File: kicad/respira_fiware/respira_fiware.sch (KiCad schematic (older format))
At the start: 14 parts, among them J1 AC PWR, J2 ES1-NO2, J3 SI7021, J4 RJ45, J5 SPS30, J6 DC PWR, U1 ESP32-NODEMCU, U2 myrra_48022

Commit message: Updating connectors and main SoC
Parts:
- J1, J6: symbol respira_fiware-rescue:Conn_01x02-gateway-rescue-gateway-rescue -> Connector_Generic:Conn_01x02
- U1: symbol respira_fiware-rescue:ESP32-NODEMCU-panstamp-gateway-rescue -> panstamp:ESP32-NODEMCU
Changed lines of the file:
@@
 $EndDescr
 $Comp
-L respira_fiware-rescue:Conn_01x02-gateway-rescue-gateway-rescue J1
+L Connector_Generic:Conn_01x02 J1
 U 1 1 5B6D72CF
 P 2000 6250
@@
 TXD0
 $Comp
-L respira_fiware-rescue:ESP32-NODEMCU-panstamp-gateway-rescue U1
+L panstamp:ESP32-NODEMCU U1
 U 1 1 5BADDDF2
 P 3200 3350
@@
 ESP32 NODEMCU board
 $Comp
-L respira_fiware-rescue:Conn_01x02-gateway-rescue-gateway-rescue J6
+L Connector_Generic:Conn_01x02 J6
 U 1 1 5D5DC69E
 P 2000 6700

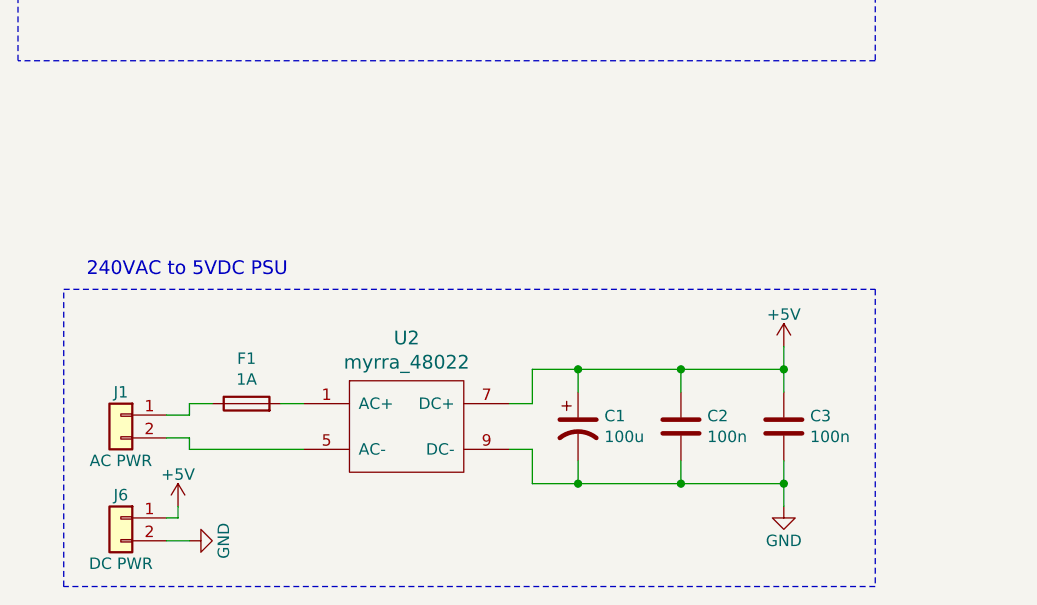
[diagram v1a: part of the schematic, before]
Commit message: Removing AC parts
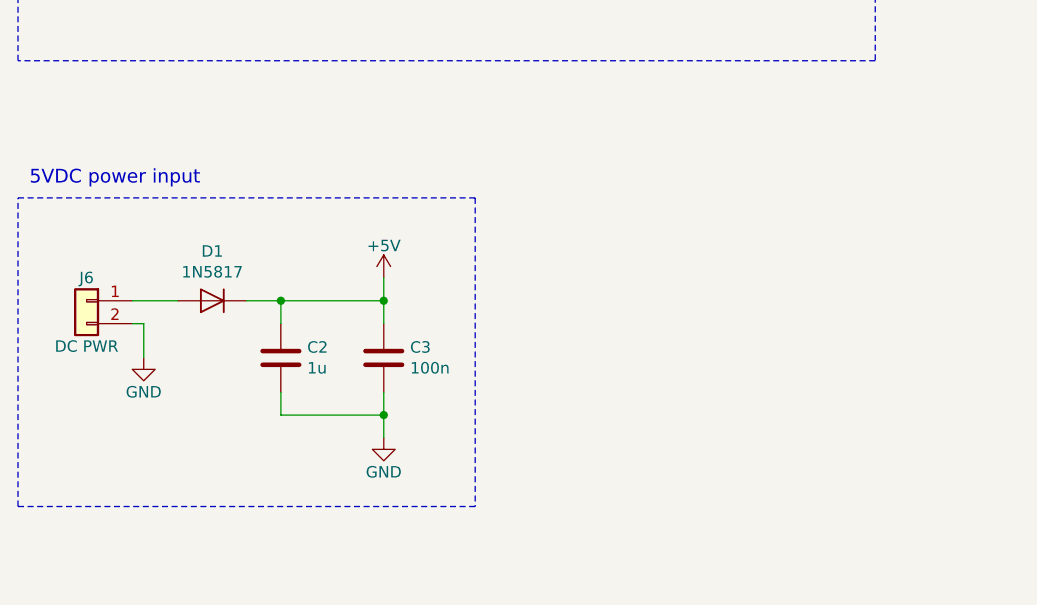
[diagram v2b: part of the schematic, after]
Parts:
- removed C1: 100u, Capacitor_THT:CP_Radial_D6.3mm_P2.50mm, symbol Device:CP1
- removed F1: 1A, mymods:litefuse_646, symbol Device:Fuse
- removed J1: AC PWR, myconnectors:terminal_block_5mm_2P, symbol Connector_Generic:Conn_01x02
- removed U2: myrra_48022, mymods:myrra_48022, symbol panstamp:myrra_48022
- added D1: 1N5817, Diode_THT:D_DO-41_SOD81_P10.16mm_Horizontal, symbol Device:D
- C2: value 100n -> 1u
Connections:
- net +5V: now also D1.1 (K); no longer J6.1 (Pin_1)
- new net: D1.2 (A), J6.1 (Pin_1)
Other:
- note added: "5VDC power input"
- note removed: "240VAC to 5VDC PSU"
- moved on the sheet: C2, C3, J6
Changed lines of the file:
@@
 $EndDescr
-$Comp
-L Connector_Generic:Conn_01x02 J1
-U 1 1 5B6D72CF
-P 2000 6250
-F 0 "J1" H 2000 6350 50  0000 C CNN
-F 1 "AC PWR" H 2000 6050 50  0000 C CNN
-F 2 "myconnectors:terminal_block_5mm_2P" H 2000 6250 50  0001 C CNN
-F 3 "" H 2000 6250 50  0001 C CNN
-	1    2000 6250
-	-1   0    0    -1
-$EndComp
 $Comp
 L power:+5V #PWR02
@@
 I2C_SDA
 $Comp
-L panstamp:myrra_48022 U2
-U 1 1 5D5AAFF8
-P 3250 6300
-F 0 "U2" H 3250 6687 60  0000 C CNN
-F 1 "myrra_48022" H 3250 6581 60  0000 C CNN
-F 2 "mymods:myrra_48022" H 3250 6300 60  0001 C CNN
-F 3 "" H 3250 6300 60  0001 C CNN
-	1    3250 6300
-	1    0    0    -1
-$EndComp
-$Comp
-L Device:Fuse F1
-U 1 1 5D5AE5C1
-P 2550 6200
-F 0 "F1" V 2747 6200 50  0000 C CNN
-F 1 "1A" V 2656 6200 50  0000 C CNN
-F 2 "mymods:litefuse_646" V 2480 6200 50  0001 C CNN
-F 3 "~" H 2550 6200 50  0001 C CNN
-	1    2550 6200
-	0    -1   -1   0
-$EndComp
-Wire Wire Line
-	2700 6200 2800 6200
-Wire Wire Line
-	2400 6200 2300 6200
-Wire Wire Line
-	2300 6200 2300 6250
-Wire Wire Line
-	2300 6250 2200 6250
-Wire Wire Line
-	2200 6350 2300 6350
-Wire Wire Line
-	2300 6350 2300 6400
-Wire Wire Line
-	2300 6400 2800 6400
-$Comp
-L Device:CP1 C1
-U 1 1 5D5AED16
-P 4000 6300
-F 0 "C1" H 4115 6346 50  0000 L CNN
-F 1 "100u" H 4115 6255 50  0000 L CNN
-F 2 "Capacitor_THT:CP_Radial_D6.3mm_P2.50mm" H 4000 6300 50  0001 C CNN
-F 3 "~" H 4000 6300 50  0001 C CNN
-	1    4000 6300
-	1    0    0    -1
-$EndComp
-Wire Wire Line
-	3700 6200 3800 6200
-Wire Wire Line
-	3800 6200 3800 6050
-Wire Wire Line
-	3800 6050 4000 6050
-Wire Wire Line
-	4000 6050 4000 6150
-Wire Wire Line
-	3700 6400 3800 6400
-Wire Wire Line
-	3800 6400 3800 6550
-Wire Wire Line
-	3800 6550 4000 6550
-Wire Wire Line
-	4000 6550 4000 6450
-$Comp
 L Device:C C2
 U 1 1 5D5AF4EF
-P 4450 6300
-F 0 "C2" H 4565 6346 50  0000 L CNN
-F 1 "100n" H 4565 6255 50  0000 L CNN
-F 2 "Capacitor_THT:C_Disc_D5.0mm_W2.5mm_P2.50mm" H 4488 6150 50  0001 C CNN
-F 3 "~" H 4450 6300 50  0001 C CNN
-	1    4450 6300
-	1    0    0    -1
-$EndComp
-Wire Wire Line
-	4000 6050 4450 6050
-Wire Wire Line
-	4450 6050 4450 6150
-Connection ~ 4000 6050
-Wire Wire Line
-	4000 6550 4450 6550
-Wire Wire Line
-	4450 6550 4450 6450
-Connection ~ 4000 6550
+P 2700 6000
+F 0 "C2" H 2815 6046 50  0000 L CNN
+F 1 "1u" H 2815 5955 50  0000 L CNN
+F 2 "Capacitor_THT:C_Disc_D5.0mm_W2.5mm_P2.50mm" H 2738 5850 50  0001 C CNN
+F 3 "~" H 2700 6000 50  0001 C CNN
+	1    2700 6000
+	1    0    0    -1
+$EndComp
+Wire Wire Line
+	2700 5750 2700 5850
+Wire Wire Line
+	2700 6250 2700 6150
 $Comp
 L power:+5V #PWR06
 U 1 1 5D5AFE82
-P 4900 5950
-F 0 "#PWR06" H 4900 5800 50  0001 C CNN
-F 1 "+5V" H 4900 6090 50  0000 C CNN
-F 2 "" H 4900 5950 50  0001 C CNN
-F 3 "" H 4900 5950 50  0001 C CNN
-	1    4900 5950
-	1    0    0    -1
-$EndComp
-Wire Wire Line
-	4900 5950 4900 6050
+P 3150 5650
+F 0 "#PWR06" H 3150 5500 50  0001 C CNN
+F 1 "+5V" H 3150 5790 50  0000 C CNN
+F 2 "" H 3150 5650 50  0001 C CNN
+F 3 "" H 3150 5650 50  0001 C CNN
+	1    3150 5650
+	1    0    0    -1
+$EndComp
+Wire Wire Line
+	3150 5650 3150 5750
 $Comp
 L power:GND #PWR07
 U 1 1 5D5B03C7
-P 4900 6650
-F 0 "#PWR07" H 4900 6400 50  0001 C CNN
-F 1 "GND" H 4900 6500 50  0000 C CNN
-F 2 "" H 4900 6650 50  0001 C CNN
-F 3 "" H 4900 6650 50  0001 C CNN
-	1    4900 6650
-	1    0    0    -1
-$EndComp
-Wire Wire Line
-	4900 6650 4900 6550
-Connection ~ 4450 6550
+P 3150 6350
+F 0 "#PWR07" H 3150 6100 50  0001 C CNN
+F 1 "GND" H 3150 6200 50  0000 C CNN
+F 2 "" H 3150 6350 50  0001 C CNN
+F 3 "" H 3150 6350 50  0001 C CNN
+	1    3150 6350
+	1    0    0    -1
+$EndComp
+Wire Wire Line
+	3150 6350 3150 6250
 $Comp
 L Device:C C3
 U 1 1 5D5B08F4
-P 4900 6300
-F 0 "C3" H 5015 6346 50  0000 L CNN
-F 1 "100n" H 5015 6255 50  0000 L CNN
-F 2 "Capacitor_THT:C_Disc_D5.0mm_W2.5mm_P2.50mm" H 4938 6150 50  0001 C CNN
-F 3 "~" H 4900 6300 50  0001 C CNN
-	1    4900 6300
-	1    0    0    -1
-$EndComp
-Wire Wire Line
-	4450 6050 4900 6050
-Connection ~ 4450 6050
-Wire Wire Line
-	4900 6050 4900 6150
-Connection ~ 4900 6050
-Wire Wire Line
-	4450 6550 4900 6550
-Wire Wire Line
-	4900 6550 4900 6450
-Connection ~ 4900 6550
+P 3150 6000
+F 0 "C3" H 3265 6046 50  0000 L CNN
+F 1 "100n" H 3265 5955 50  0000 L CNN
+F 2 "Capacitor_THT:C_Disc_D5.0mm_W2.5mm_P2.50mm" H 3188 5850 50  0001 C CNN
+F 3 "~" H 3150 6000 50  0001 C CNN
+	1    3150 6000
+	1    0    0    -1
+$EndComp
+Wire Wire Line
+	2700 5750 3150 5750
+Wire Wire Line
+	3150 5750 3150 5850
+Connection ~ 3150 5750
+Wire Wire Line
+	2700 6250 3150 6250
+Wire Wire Line
+	3150 6250 3150 6150
+Connection ~ 3150 6250
 $Comp
 L Device:R R1
@@
 Text Notes 6750 4450 0    60   ~ 0
 SI7021 Temperature-Humidity sensor
-Wire Notes Line
-	5300 5700 5300 7000
-Wire Notes Line
-	5300 7000 1750 7000
-Wire Notes Line
-	1750 7000 1750 5700
-Wire Notes Line
-	1750 5700 5300 5700
-Text Notes 1850 5650 0    60   ~ 0
-240VAC to 5VDC PSU
+Text Notes 1600 5250 0    60   ~ 0
+5VDC power input
 $Comp
 L Connector_Generic:Conn_01x05 J5
@@
 L Connector_Generic:Conn_01x02 J6
 U 1 1 5D5DC69E
-P 2000 6700
-F 0 "J6" H 2000 6800 50  0000 C CNN
-F 1 "DC PWR" H 2000 6500 50  0000 C CNN
-F 2 "myconnectors:terminal_block_5mm_2P" H 2000 6700 50  0001 C CNN
-F 3 "" H 2000 6700 50  0001 C CNN
-	1    2000 6700
+P 1850 5750
+F 0 "J6" H 1850 5850 50  0000 C CNN
+F 1 "DC PWR" H 1850 5550 50  0000 C CNN
+F 2 "myconnectors:terminal_block_5mm_2P" H 1850 5750 50  0001 C CNN
+F 3 "" H 1850 5750 50  0001 C CNN
+	1    1850 5750
 	-1   0    0    -1
 $EndComp
 $Comp
-L power:+5V #PWR018
-U 1 1 5D5DF703
-P 2250 6650
-F 0 "#PWR018" H 2250 6500 50  0001 C CNN
-F 1 "+5V" H 2250 6790 50  0000 C CNN
-F 2 "" H 2250 6650 50  0001 C CNN
-F 3 "" H 2250 6650 50  0001 C CNN
-	1    2250 6650
-	1    0    0    -1
-$EndComp
-Wire Wire Line
-	2200 6700 2250 6700
-Wire Wire Line
-	2250 6700 2250 6650
+L Device:D D1
+U 1 1 5D6CF32E
+P 2400 5750
+F 0 "D1" H 2400 5534 50  0000 C CNN
+F 1 "1N5817" H 2400 5625 50  0000 C CNN
+F 2 "Diode_THT:D_DO-41_SOD81_P10.16mm_Horizontal" H 2400 5750 50  0001 C CNN
+F 3 "~" H 2400 5750 50  0001 C CNN
+	1    2400 5750
+	-1   0    0    1
+$EndComp
+Wire Wire Line
+	2550 5750 2700 5750
+Connection ~ 2700 5750
 $Comp
 L power:GND #PWR019
 U 1 1 5D5E0FDF
-P 2300 6800
-F 0 "#PWR019" H 2300 6550 50  0001 C CNN
-F 1 "GND" H 2300 6650 50  0000 C CNN
-F 2 "" H 2300 6800 50  0001 C CNN
-F 3 "" H 2300 6800 50  0001 C CNN
-	1    2300 6800
-	0    -1   -1   0
-$EndComp
-Wire Wire Line
-	2200 6800 2300 6800
+P 2100 6000
+F 0 "#PWR019" H 2100 5750 50  0001 C CNN
+F 1 "GND" H 2100 5850 50  0000 C CNN
+F 2 "" H 2100 6000 50  0001 C CNN
+F 3 "" H 2100 6000 50  0001 C CNN
+	1    2100 6000
+	1    0    0    -1
+$EndComp
+Wire Wire Line
+	2250 5750 2050 5750
+Wire Wire Line
+	2050 5850 2100 5850
+Wire Wire Line
+	2100 5850 2100 6000
+Wire Notes Line
+	3550 5300 3550 6650
+Wire Notes Line
+	3550 6650 1550 6650
+Wire Notes Line
+	1550 6650 1550 5300
+Wire Notes Line
+	1550 5300 3550 5300
 $EndSCHEMATC

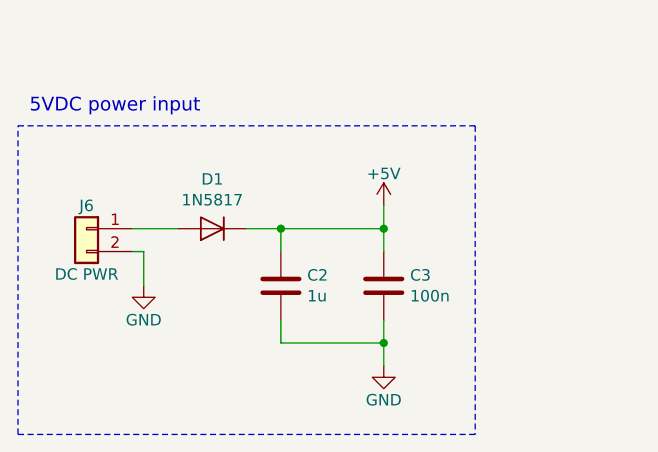
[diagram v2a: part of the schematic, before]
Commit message: D1 removed
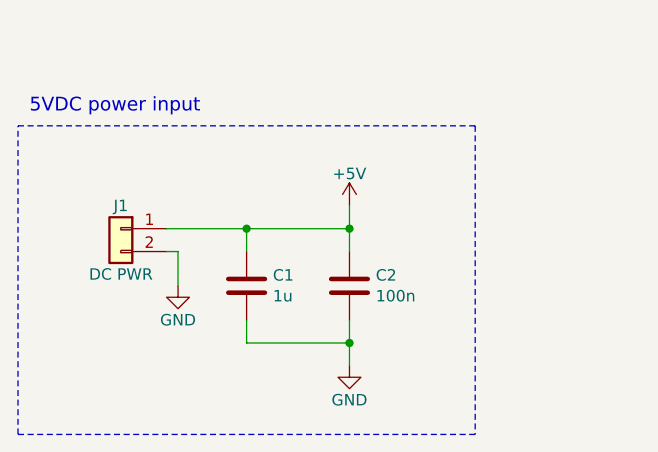
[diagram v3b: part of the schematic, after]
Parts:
- removed D1: 1N5817, Diode_THT:D_DO-41_SOD81_P10.16mm_Horizontal, symbol Device:D
- renumbered C2 to C1, C3 to C2, J6 to J1
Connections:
- net +5V: now also J1.1 (Pin_1)
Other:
- moved on the sheet: C1, C2, J1
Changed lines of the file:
@@
 I2C_SDA
 $Comp
-L Device:C C2
+L Device:C C1
 U 1 1 5D5AF4EF
-P 2700 6000
-F 0 "C2" H 2815 6046 50  0000 L CNN
-F 1 "1u" H 2815 5955 50  0000 L CNN
-F 2 "Capacitor_THT:C_Disc_D5.0mm_W2.5mm_P2.50mm" H 2738 5850 50  0001 C CNN
-F 3 "~" H 2700 6000 50  0001 C CNN
-	1    2700 6000
-	1    0    0    -1
-$EndComp
-Wire Wire Line
-	2700 5750 2700 5850
-Wire Wire Line
-	2700 6250 2700 6150
+P 2550 6000
+F 0 "C1" H 2665 6046 50  0000 L CNN
+F 1 "1u" H 2665 5955 50  0000 L CNN
+F 2 "Capacitor_THT:C_Disc_D5.0mm_W2.5mm_P2.50mm" H 2588 5850 50  0001 C CNN
+F 3 "~" H 2550 6000 50  0001 C CNN
+	1    2550 6000
+	1    0    0    -1
+$EndComp
+Wire Wire Line
+	2550 5750 2550 5850
+Wire Wire Line
+	2550 6250 2550 6150
 $Comp
 L power:+5V #PWR06
 U 1 1 5D5AFE82
-P 3150 5650
-F 0 "#PWR06" H 3150 5500 50  0001 C CNN
-F 1 "+5V" H 3150 5790 50  0000 C CNN
-F 2 "" H 3150 5650 50  0001 C CNN
-F 3 "" H 3150 5650 50  0001 C CNN
-	1    3150 5650
-	1    0    0    -1
-$EndComp
-Wire Wire Line
-	3150 5650 3150 5750
+P 3000 5650
+F 0 "#PWR06" H 3000 5500 50  0001 C CNN
+F 1 "+5V" H 3000 5790 50  0000 C CNN
+F 2 "" H 3000 5650 50  0001 C CNN
+F 3 "" H 3000 5650 50  0001 C CNN
+	1    3000 5650
+	1    0    0    -1
+$EndComp
+Wire Wire Line
+	3000 5650 3000 5750
 $Comp
 L power:GND #PWR07
 U 1 1 5D5B03C7
-P 3150 6350
-F 0 "#PWR07" H 3150 6100 50  0001 C CNN
-F 1 "GND" H 3150 6200 50  0000 C CNN
-F 2 "" H 3150 6350 50  0001 C CNN
-F 3 "" H 3150 6350 50  0001 C CNN
-	1    3150 6350
-	1    0    0    -1
-$EndComp
-Wire Wire Line
-	3150 6350 3150 6250
-$Comp
-L Device:C C3
+P 3000 6350
+F 0 "#PWR07" H 3000 6100 50  0001 C CNN
+F 1 "GND" H 3000 6200 50  0000 C CNN
+F 2 "" H 3000 6350 50  0001 C CNN
+F 3 "" H 3000 6350 50  0001 C CNN
+	1    3000 6350
+	1    0    0    -1
+$EndComp
+Wire Wire Line
+	3000 6350 3000 6250
+$Comp
+L Device:C C2
 U 1 1 5D5B08F4
-P 3150 6000
-F 0 "C3" H 3265 6046 50  0000 L CNN
-F 1 "100n" H 3265 5955 50  0000 L CNN
-F 2 "Capacitor_THT:C_Disc_D5.0mm_W2.5mm_P2.50mm" H 3188 5850 50  0001 C CNN
-F 3 "~" H 3150 6000 50  0001 C CNN
-	1    3150 6000
-	1    0    0    -1
-$EndComp
-Wire Wire Line
-	2700 5750 3150 5750
-Wire Wire Line
-	3150 5750 3150 5850
-Connection ~ 3150 5750
-Wire Wire Line
-	2700 6250 3150 6250
-Wire Wire Line
-	3150 6250 3150 6150
-Connection ~ 3150 6250
+P 3000 6000
+F 0 "C2" H 3115 6046 50  0000 L CNN
+F 1 "100n" H 3115 5955 50  0000 L CNN
+F 2 "Capacitor_THT:C_Disc_D5.0mm_W2.5mm_P2.50mm" H 3038 5850 50  0001 C CNN
+F 3 "~" H 3000 6000 50  0001 C CNN
+	1    3000 6000
+	1    0    0    -1
+$EndComp
+Wire Wire Line
+	2550 5750 3000 5750
+Wire Wire Line
+	3000 5750 3000 5850
+Connection ~ 3000 5750
+Wire Wire Line
+	2550 6250 3000 6250
+Wire Wire Line
+	3000 6250 3000 6150
+Connection ~ 3000 6250
 $Comp
 L Device:R R1
@@
 ESP32 NODEMCU board
 $Comp
-L Connector_Generic:Conn_01x02 J6
+L Connector_Generic:Conn_01x02 J1
 U 1 1 5D5DC69E
-P 1850 5750
-F 0 "J6" H 1850 5850 50  0000 C CNN
-F 1 "DC PWR" H 1850 5550 50  0000 C CNN
-F 2 "myconnectors:terminal_block_5mm_2P" H 1850 5750 50  0001 C CNN
-F 3 "" H 1850 5750 50  0001 C CNN
-	1    1850 5750
+P 2000 5750
+F 0 "J1" H 2000 5850 50  0000 C CNN
+F 1 "DC PWR" H 2000 5550 50  0000 C CNN
+F 2 "myconnectors:terminal_block_5mm_2P" H 2000 5750 50  0001 C CNN
+F 3 "" H 2000 5750 50  0001 C CNN
+	1    2000 5750
 	-1   0    0    -1
 $EndComp
-$Comp
-L Device:D D1
-U 1 1 5D6CF32E
-P 2400 5750
-F 0 "D1" H 2400 5534 50  0000 C CNN
-F 1 "1N5817" H 2400 5625 50  0000 C CNN
-F 2 "Diode_THT:D_DO-41_SOD81_P10.16mm_Horizontal" H 2400 5750 50  0001 C CNN
-F 3 "~" H 2400 5750 50  0001 C CNN
-	1    2400 5750
-	-1   0    0    1
-$EndComp
-Wire Wire Line
-	2550 5750 2700 5750
-Connection ~ 2700 5750
+Connection ~ 2550 5750
 $Comp
 L power:GND #PWR019
 U 1 1 5D5E0FDF
-P 2100 6000
-F 0 "#PWR019" H 2100 5750 50  0001 C CNN
-F 1 "GND" H 2100 5850 50  0000 C CNN
-F 2 "" H 2100 6000 50  0001 C CNN
-F 3 "" H 2100 6000 50  0001 C CNN
-	1    2100 6000
-	1    0    0    -1
-$EndComp
-Wire Wire Line
-	2250 5750 2050 5750
-Wire Wire Line
-	2050 5850 2100 5850
-Wire Wire Line
-	2100 5850 2100 6000
+P 2250 6000
+F 0 "#PWR019" H 2250 5750 50  0001 C CNN
+F 1 "GND" H 2250 5850 50  0000 C CNN
+F 2 "" H 2250 6000 50  0001 C CNN
+F 3 "" H 2250 6000 50  0001 C CNN
+	1    2250 6000
+	1    0    0    -1
+$EndComp
+Wire Wire Line
+	2200 5850 2250 5850
+Wire Wire Line
+	2250 5850 2250 6000
 Wire Notes Line
 	3550 5300 3550 6650
@@
 Wire Notes Line
 	1550 5300 3550 5300
+Wire Wire Line
+	2200 5750 2550 5750
 $EndSCHEMATC
